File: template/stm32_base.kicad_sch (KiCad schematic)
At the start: 41 parts, among them J1 Network Connector, J3 STDC14 STLink connector, SW1 SW_Push, U1 LD39050PU33R, U2 STM32G474RBT6, U3 SN65HVD230, Y1 8MHz

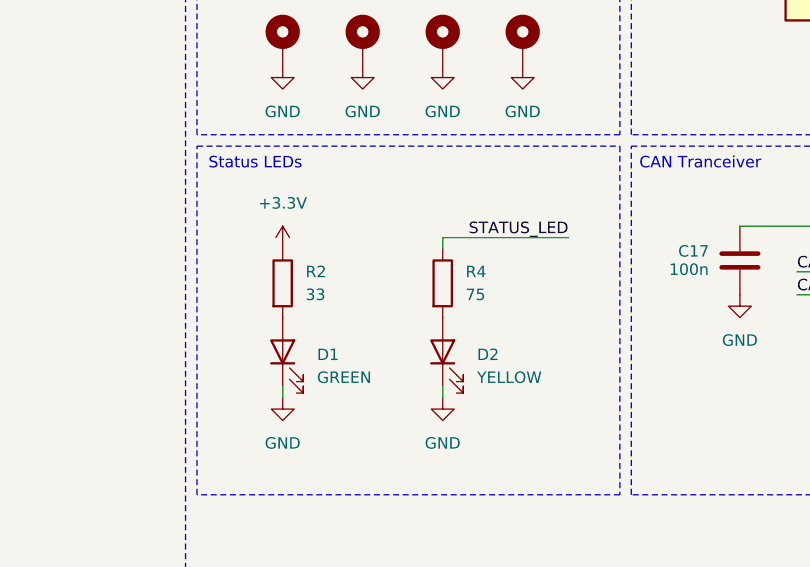
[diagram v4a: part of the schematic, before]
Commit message: Remove CAN Resistor and change the values of the LED resistors
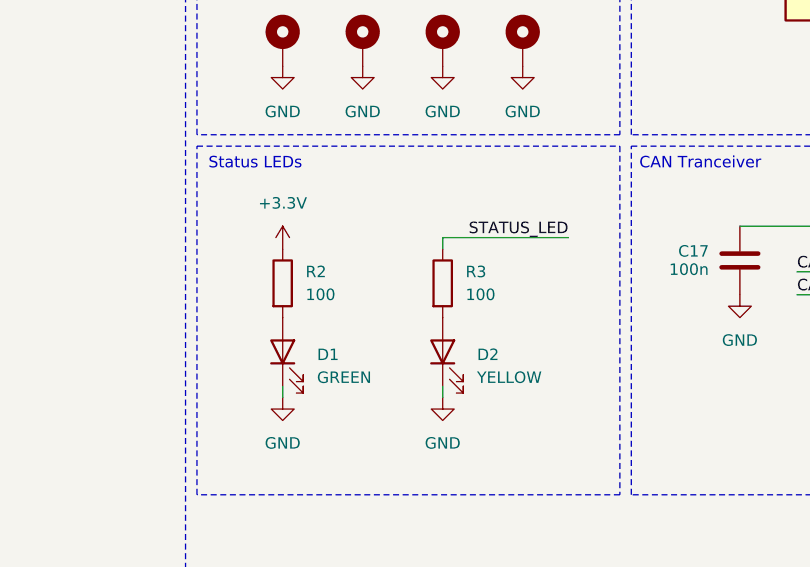
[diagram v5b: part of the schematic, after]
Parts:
- removed R4: 75, Resistor_SMD:R_0603_1608Metric, symbol Device:R
- added R3: 100, Resistor_SMD:R_0603_1608Metric, symbol Device:R
- R2: value 33 -> 100; JLCPCB C23140 -> C22775
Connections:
- net STATUS_LED: now also R3.1
- net at D2.2 (A): now also R3.2
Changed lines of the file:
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@@
 			)
 		)
-		(property "Value" "33"
+		(property "Value" "100"
 			(at 189.23 134.6199 0)
 			(effects
@@
 			)
 		)
-		(property "JLCPCB" "C23140"
+		(property "JLCPCB" "C22775"
 			(at 186.69 133.35 0)
 			(effects
@@
 	)
 	(symbol
+		(lib_id "Device:R")
+		(at 204.47 133.35 0)
+		(unit 1)
+		(exclude_from_sim no)
+		(in_bom yes)
+		(on_board yes)
+		(dnp no)
+		(fields_autoplaced yes)
+		(property "Reference" "R3"
+			(at 207.01 132.0799 0)
+			(effects
+				(font
+					(size 1.27 1.27)
+				)
+				(justify left)
+			)
+		)
+		(property "Value" "100"
+			(at 207.01 134.6199 0)
+			(effects
+				(font
+					(size 1.27 1.27)
+				)
+				(justify left)
+			)
+		)
+		(property "Footprint" "Resistor_SMD:R_0603_1608Metric"
+			(at 202.692 133.35 90)
+			(effects
+				(font
+					(size 1.27 1.27)
+				)
+				(hide yes)
+			)
+		)
+		(property "Datasheet" "~"
+			(at 204.47 133.35 0)
+			(effects
+				(font
+					(size 1.27 1.27)
+				)
+				(hide yes)
+			)
+		)
+		(property "Description" "Resistor"
+			(at 204.47 133.35 0)
+			(effects
+				(font
+					(size 1.27 1.27)
+				)
+				(hide yes)
+			)
+		)
+		(property "JLCPCB" "C22775"
+			(at 204.47 133.35 0)
+			(effects
+				(font
+					(size 1.27 1.27)
+				)
+				(hide yes)
+			)
+		)
+		(pin "1"
+		)
+		(pin "2"
+		)
+		(instances
+			(project "template"
+				(path "/4b4cf3aa-c94c-4150-b9c5-35049cd71136/7d59fd70-1fff-4c9c-ae77-583b08aef567"
+					(reference "R3")
+					(unit 1)
+				)
+			)
+		)
+	)
+	(symbol
 		(lib_id "Switch:SW_Push")
 		(at 146.05 45.72 0)
@@
 					(unit 1)
 				)
-			)
-		)
-	)
-	(symbol
-		(lib_id "Device:R")
-		(at 204.47 133.35 0)
-		(unit 1)
-		(exclude_from_sim no)
-		(in_bom yes)
-		(on_board yes)
-		(dnp no)
-		(fields_autoplaced yes)
-		(property "Reference" "R4"
-			(at 207.01 132.0799 0)
-			(effects
-				(font
-					(size 1.27 1.27)
-				)
-				(justify left)
-			)
-		)
-		(property "Value" "75"
-			(at 207.01 134.6199 0)
-			(effects
-				(font
-					(size 1.27 1.27)
-				)
-				(justify left)
-			)
-		)
-		(property "Footprint" "Resistor_SMD:R_0603_1608Metric"
-			(at 202.692 133.35 90)
-			(effects
-				(font
-					(size 1.27 1.27)
-				)
-				(hide yes)
-			)
-		)
-		(property "Datasheet" "~"
-			(at 204.47 133.35 0)
-			(effects
-				(font
-					(size 1.27 1.27)
-				)
-				(hide yes)
-			)
-		)
-		(property "Description" "Resistor"
-			(at 204.47 133.35 0)
-			(effects
-				(font
-					(size 1.27 1.27)
-				)
-				(hide yes)
-			)
-		)
-		(property "JLCPCB" "C4275"
-			(at 204.47 133.35 0)
-			(effects
-				(font
-					(size 1.27 1.27)
-				)
-				(hide yes)
-			)
-		)
-		(pin "1"
-		)
-		(pin "2"
-		)
-		(instances
-			(project "template"
-				(path "/4b4cf3aa-c94c-4150-b9c5-35049cd71136/7d59fd70-1fff-4c9c-ae77-583b08aef567"
-					(reference "R4")
-					(unit 1)
-				)
